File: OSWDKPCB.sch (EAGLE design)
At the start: 55 parts, among them IC1 S08AC60, IC2 S08JS16, IC3 BUFF, IC4 BUFF, IC7 NCP1117ST50T3G, P0 HDR-8, P1 HDR-8, P2 HDR-8, P3 HDR-8, U1 PMV160UP, U3 LP2985-33DBVR, Y1 4MHz, Y2 12MHz

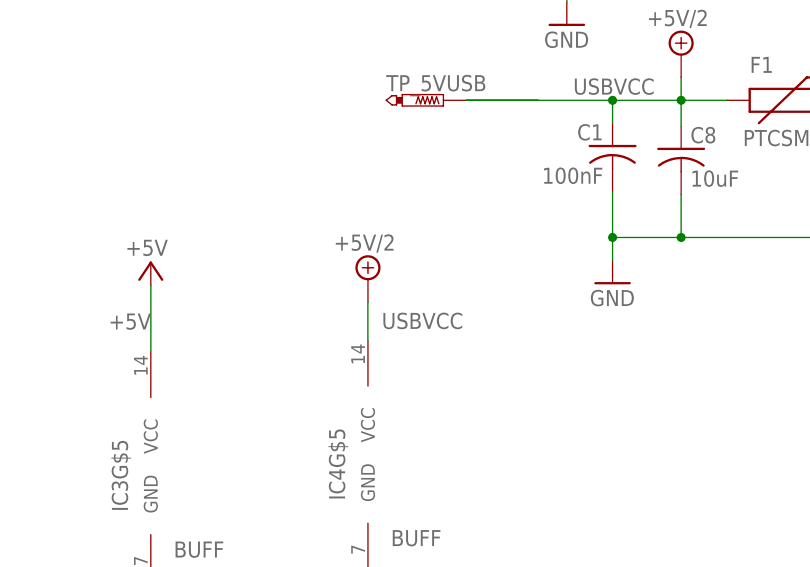
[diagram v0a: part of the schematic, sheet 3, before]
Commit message: VCC de los buffer
La alimentación de ambos buffers se ha cambiado a 5V de la tarjeta.
El logo de la parte trasera se ha actualizado a un simbolo.
La revision ha cambiado a 4.00
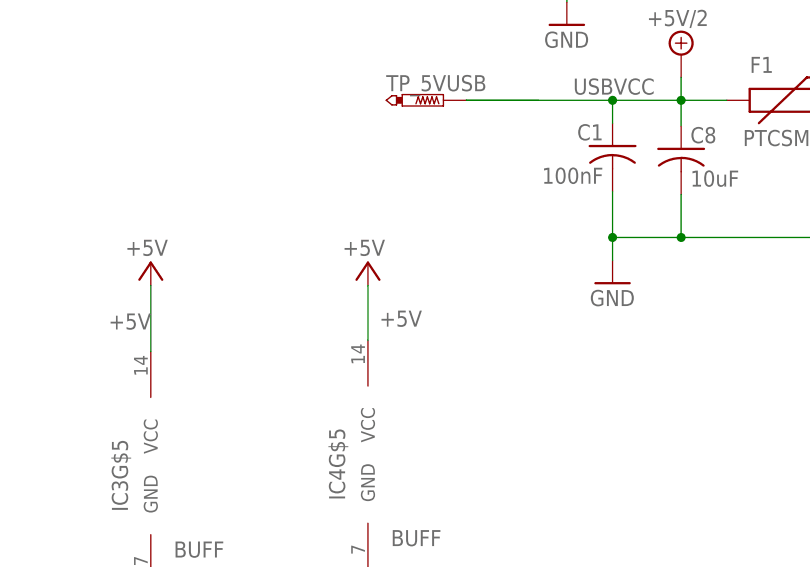
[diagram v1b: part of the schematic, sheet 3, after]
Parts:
- added U$2: OSWDK_BACK_LOGO, OSWarrior:OSWDK_BACK_LOGO
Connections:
- net +5V: now also IC4G$5.VCC
- net USBVCC: no longer IC4G$5.VCC
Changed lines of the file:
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@@
 <part name="R11" library="resistor" deviceset="R-US_" device="M0805" value="33"/>
 <part name="GND7" library="supply1" deviceset="GND" device=""/>
-<part name="P+7" library="supply2" deviceset="+5V/2" device="" value="+5V/2"/>
 <part name="TP_BKGD" library="testpad" deviceset="PTR1" device="B1,27"/>
 <part name="TP_RST" library="testpad" deviceset="PTR1" device="B1,27">
@@
 <part name="P+8" library="supply1" deviceset="+5V" device="" value="+5V"/>
 <part name="U$1" library="OSWarrior" deviceset="OSWDK_LOGO" device=""/>
+<part name="P+7" library="supply1" deviceset="+5V" device="" value="+5V"/>
+<part name="U$2" library="OSWarrior" deviceset="OSWDK_BACK_LOGO" device=""/>
 </parts>
 <sheets>
@@
 <attribute name="VALUE" x="212.725" y="106.68" size="1.778" layer="96" rot="R180"/>
 </instance>
-<instance part="U$1" gate="G$1" x="58.42" y="50.8"/>
+<instance part="U$1" gate="G$1" x="106.68" y="48.26"/>
+<instance part="U$2" gate="G$1" x="5.08" y="48.26"/>
 </instances>
 <busses>
@@
 <instance part="R11" gate="G$1" x="218.7575" y="114.3" rot="R90"/>
 <instance part="GND7" gate="1" x="155.702" y="46.355"/>
-<instance part="P+7" gate="G$1" x="155.702" y="84.2645"/>
 <instance part="TP_BKGD" gate="G$1" x="25.4" y="124.46" rot="R270"/>
 <instance part="TP_RST" gate="G$1" x="8.89" y="21.59" rot="R270"/>
@@
 <instance part="P+8" gate="1" x="7.62" y="147.32" smashed="yes">
 <attribute name="VALUE" x="9.525" y="149.86" size="1.778" layer="96" rot="R180"/>
+</instance>
+<instance part="P+7" gate="1" x="155.702" y="86.106" smashed="yes">
+<attribute name="VALUE" x="157.607" y="88.646" size="1.778" layer="96" rot="R180"/>
 </instance>
 </instances>
@@
 <label x="101.9175" y="160.9725" size="1.778" layer="95"/>
 </segment>
-<segment>
-<pinref part="P+7" gate="G$1" pin="+5V/2"/>
-<wire x1="155.702" y1="81.7245" x2="155.702" y2="77.47" width="0.1524" layer="91"/>
-<pinref part="IC4" gate="G$5" pin="VCC"/>
-<label x="157.226" y="78.74" size="1.778" layer="95"/>
-</segment>
 </net>
 <net name="+5V" class="1">
@@
 <label x="10.16" y="142.24" size="1.778" layer="95"/>
 </segment>
-</net>
+<segment>
+<pinref part="P+7" gate="1" pin="+5V"/>
+<pinref part="IC4" gate="G$5" pin="VCC"/>
+<wire x1="155.702" y1="83.566" x2="155.702" y2="77.47" width="0.1524" layer="91"/>
+<label x="156.972" y="78.994" size="1.778" layer="95"/>
+</segment>
+</net>

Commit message: Version 4.2
Revision 3.0
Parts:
- removed TP_BKGD: PTR1B1,27, testpad:PTR1B1,27
- added BDM_EN: (no value), jumper:SJ
- added TP_BKGD1: PTR1B1,27, testpad:PTR1B1,27
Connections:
- new net N$6: BDM_EN.2, IC1.BKGD/MS, TP_BKGD1.TP
- net BKGD: now also BDM_EN.1; no longer IC1.BKGD/MS, TP_BKGD.TP
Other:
- note added: "+5V Regulator"
- moved on the sheet: IC1, R6, R8, TP_5V, TP_GND, TP_MCLK, TP_RST, TP_RX, TP_TPMCLK, TP_TX
